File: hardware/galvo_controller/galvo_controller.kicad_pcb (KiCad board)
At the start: 4 copper layers, 70 x 90 mm, 121 parts, among them J1 USB_OTG, J2 Conn_01x03, J3 Conn_01x03, J4 Micro_SD_Card_Det, J5 Red, J6 White, J7 Conn_01x03, J8 Conn_01x03, Q1 MMBT2222, Q2 MMBT2222, U1 SN74LV1T34, U2 ESP-WROOM-32D, U3 CP2104, U4 TPS54295PWP, U5 PCM3060, U6 NCP1117LP, U7 OPA2134, U8 LME49724, U9 LME49724

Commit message: Working on layout
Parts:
- moved JP1 64.2 mm to (163.9, 83.0), turned to 180 degrees
- moved JP2 49.4 mm to (178.0, 105.5), turned to 90 degrees
- moved R9 46.5 mm to (152.2, 117.3), turned to 270 degrees
- moved R15 46.1 mm to (175.4, 111.6), turned to 270 degrees
- moved C4 45.9 mm to (155.7, 112.9), turned to 180 degrees
- moved R18 45.0 mm to (167.0, 111.6), turned to 270 degrees
- moved R5 44.3 mm to (155.1, 85.5), turned to 270 degrees
- moved R14 42.3 mm to (177.2, 111.6), turned to 270 degrees
- moved R17 41.0 mm to (168.8, 111.6), turned to 270 degrees
- moved R7 40.8 mm to (151.3, 85.5), turned to 270 degrees
- moved C26 40.8 mm to (173.0, 111.4), turned to 90 degrees
- moved R13 40.2 mm to (179.0, 111.6), turned to 270 degrees
- moved R8 39.7 mm to (146.4, 117.3), turned to 90 degrees
- moved C2 38.6 mm to (151.5, 112.3)
- moved Q1 38.4 mm to (149.3, 115.3), turned to 90 degrees
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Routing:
- net /SD_DAT1: track 0.00 -> 43.2 mm
- net /SD_CMD: track 0.00 -> 39.2 mm, vias 0 -> 2
- net /SD_DAT0: track 0.00 -> 38.2 mm
- net /VOUTL_N: track 0.00 -> 36.8 mm, vias 0 -> 2
- net /VOUTL_P: track 0.00 -> 35.3 mm
- net /SD_DAT2: track 0.00 -> 32.9 mm, vias 0 -> 2
- net /SD_DAT3: track 0.00 -> 32.3 mm, vias 0 -> 2
- net +3V3: track 3.01 -> 31.3 mm, vias 1 -> 8
- net /SD_CLK: track 0.00 -> 28.0 mm, vias 0 -> 2
- net Net-(JP2-Pad1): track 0.00 -> 17.5 mm, vias 0 -> 2
- net Net-(D2-Pad1): track 0.00 -> 16.7 mm, vias 0 -> 2
- net Net-(D1-Pad1): track 0.00 -> 15.8 mm, vias 0 -> 2
- net /VOUTR_P: track 0.00 -> 14.2 mm
- net /VOUTR_N: track 0.00 -> 14.2 mm
- net /VBUS: track 0.00 -> 12.1 mm, vias 0 -> 2
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
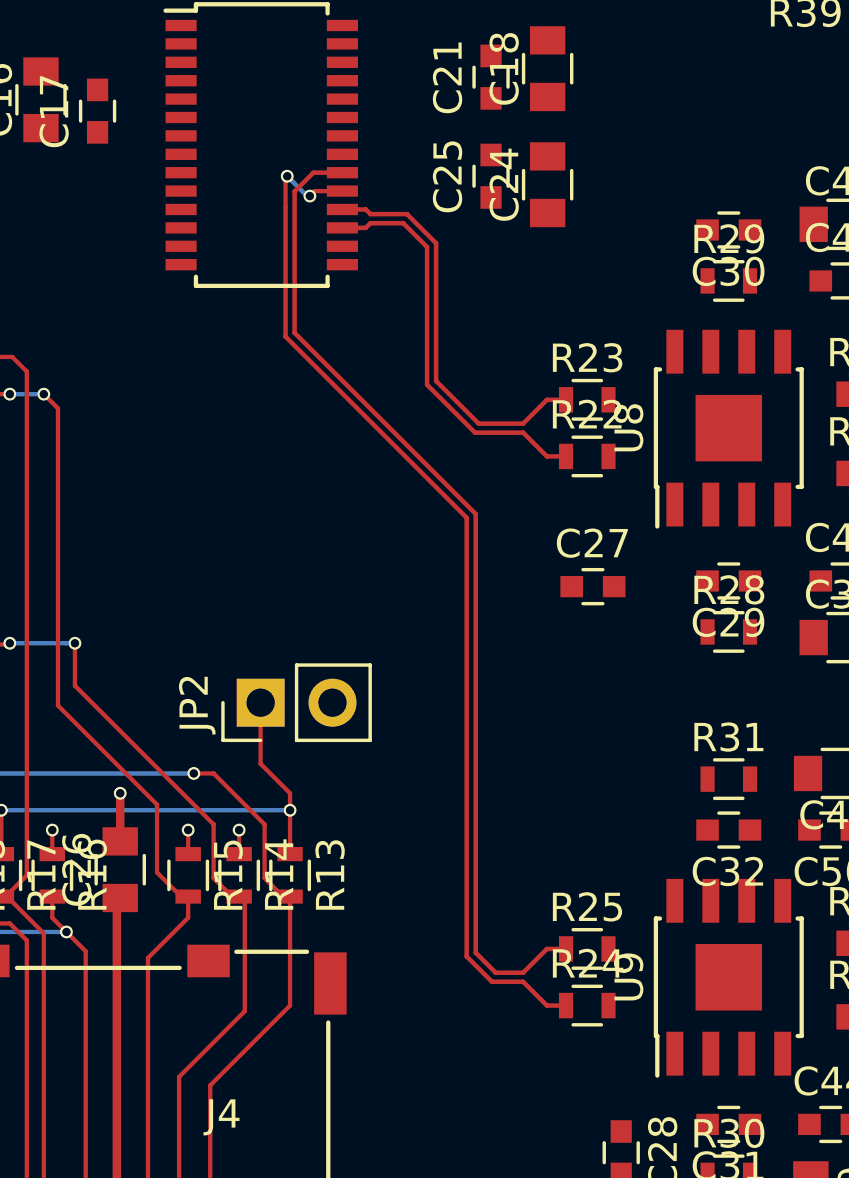
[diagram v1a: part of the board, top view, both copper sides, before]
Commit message: Swapped input L/R channels
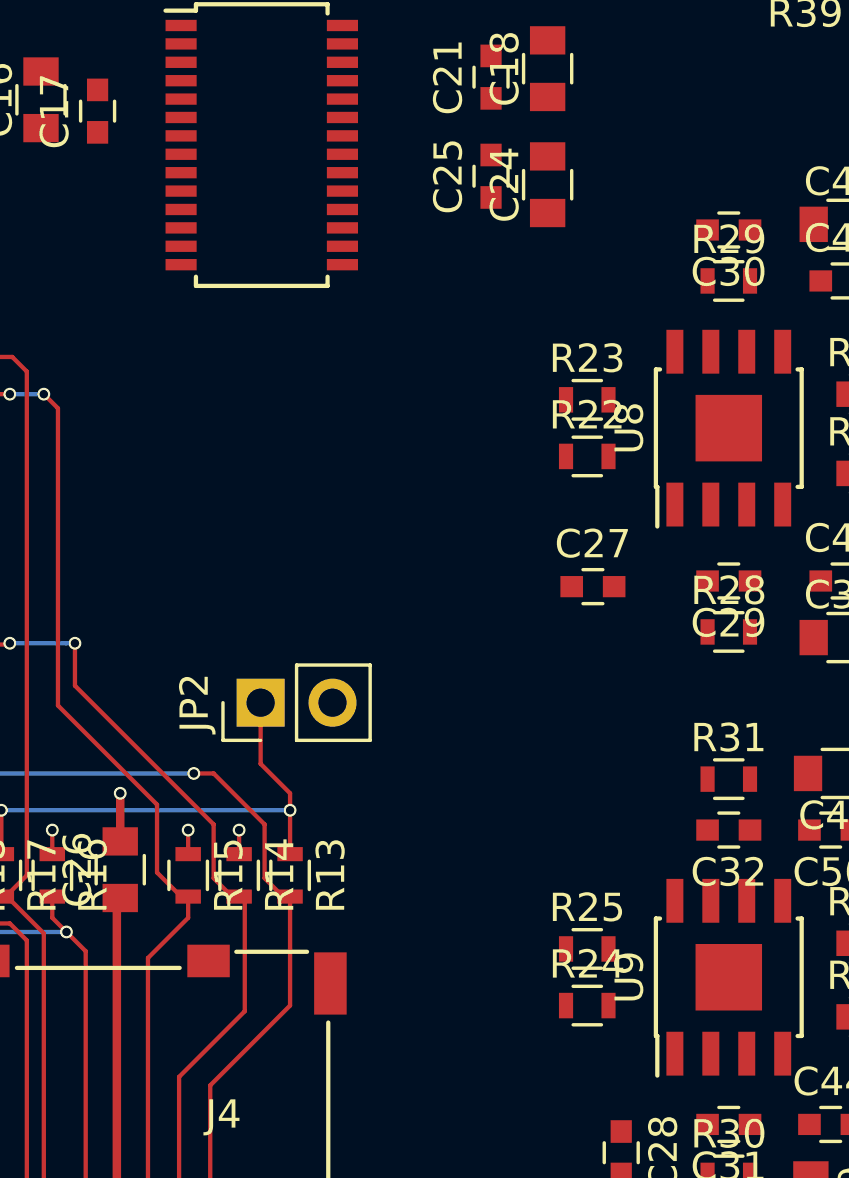
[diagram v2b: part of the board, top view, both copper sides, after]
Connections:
- net Net-(D4-Pad3) renamed /VINR
- net Net-(D5-Pad3) renamed /VINL
- R22 pad 1: /VOUTR_N -> /VOUTL_N
- R23 pad 1: /VOUTR_P -> /VOUTL_P
- R24 pad 1: /VOUTL_N -> /VOUTR_N
- R25 pad 1: /VOUTL_P -> /VOUTR_P
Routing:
- net /VOUTL_N: track 36.8 -> 0.00 mm, vias 2 -> 0
- net /VOUTL_P: track 35.3 -> 0.00 mm
- net /VOUTR_P: track 14.2 -> 0.00 mm
- net /VOUTR_N: track 14.2 -> 0.00 mm

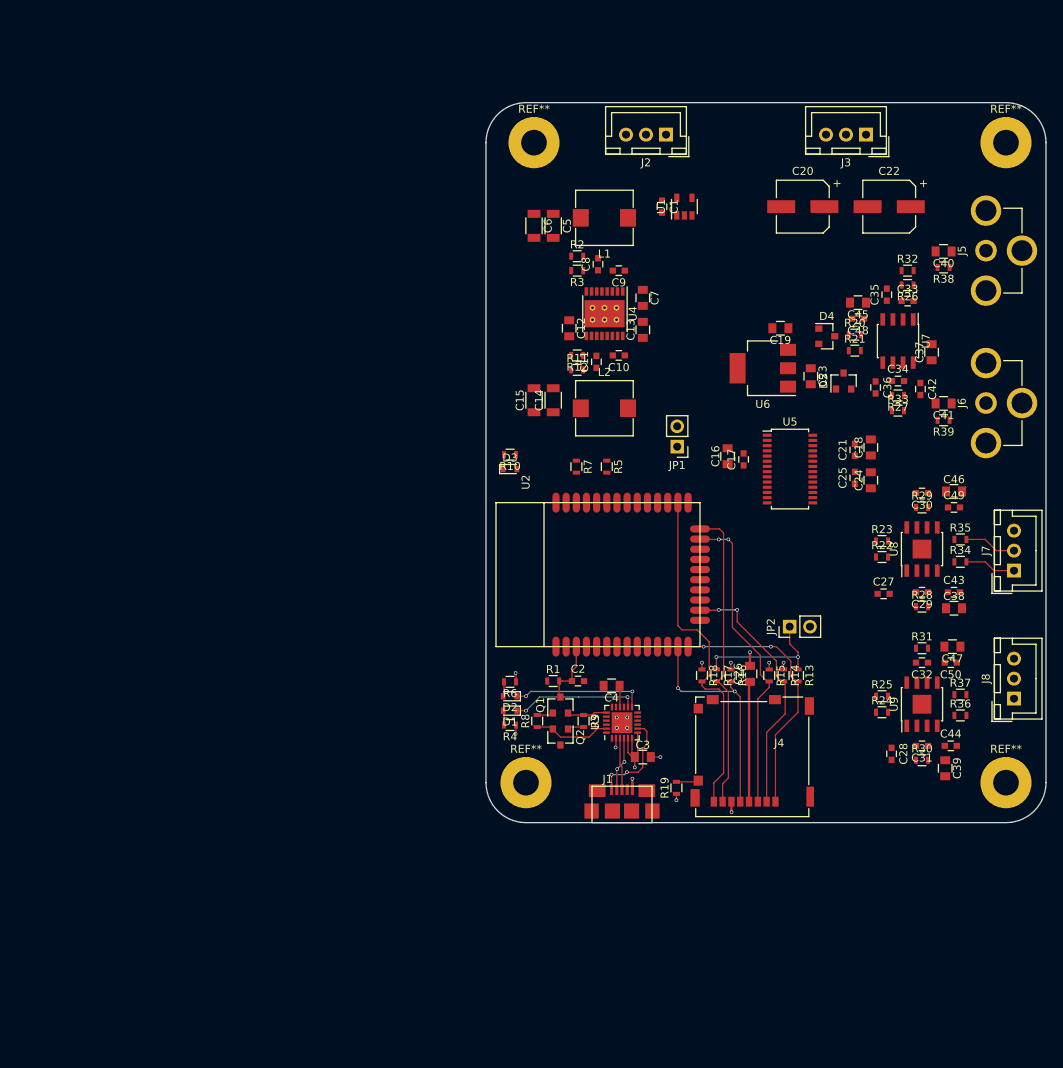
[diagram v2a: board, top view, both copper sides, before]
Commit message: Added OLED and nav switch
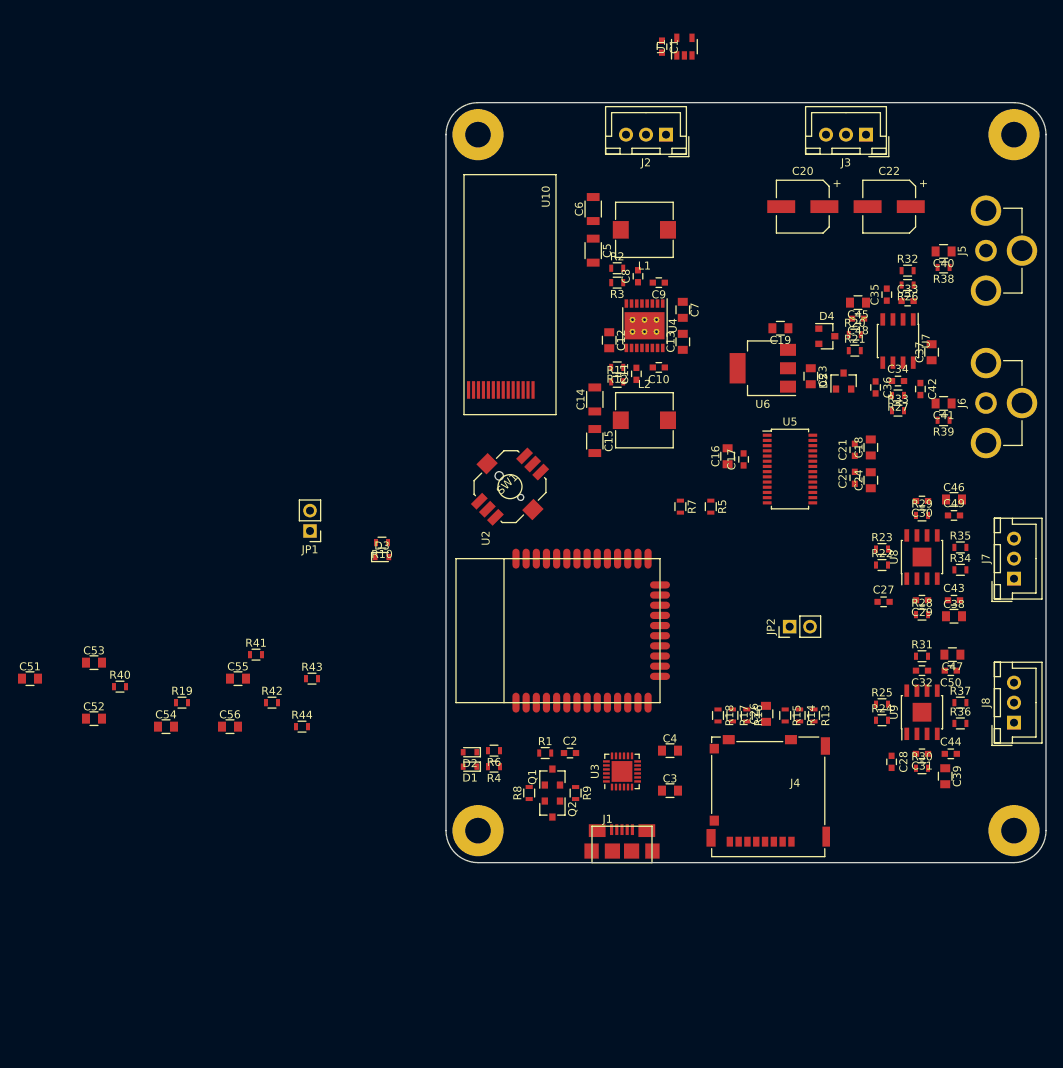
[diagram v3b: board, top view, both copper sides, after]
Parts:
- removed the REF** at (146.0, 45.0)
- removed the REF** at (205.0, 45.0)
- removed the REF** at (205.0, 125.0)
- removed the REF** at (145.0, 125.0)
- added C51: 1u, Capacitors_SMD:C_0805, F.Cu at (83.0, 112.0)
- added C52: 1u, Capacitors_SMD:C_0805, F.Cu at (91.0, 117.0)
- added C53: 10u, Capacitors_SMD:C_0805, F.Cu at (91.0, 110.0)
- added C54: 1u, Capacitors_SMD:C_0805, F.Cu at (100.0, 118.0)
- added C55: 1u, Capacitors_SMD:C_0805, F.Cu at (109.0, 112.0)
- added C56: 10u, Capacitors_SMD:C_0805, F.Cu at (108.0, 118.0)
- added R40: 10k, Resistors_SMD:R_0603, F.Cu at (94.2, 113.0)
- added R41: 10k, Resistors_SMD:R_0603, F.Cu at (111.2, 109.0)
- added R42: 10k, Resistors_SMD:R_0603, F.Cu at (113.2, 115.0)
- added R43: 10k, Resistors_SMD:R_0603, F.Cu at (118.2, 112.0)
- added R44: 10k, Resistors_SMD:R_0603, F.Cu at (117.0, 118.0)
- added REF**: MountingHole_3.2mm_M3_Pad, Mounting_Holes:MountingHole_3.2mm_M3_Pad, F.Cu at (139.0, 131.0)
- added REF**: MountingHole_3.2mm_M3_Pad, Mounting_Holes:MountingHole_3.2mm_M3_Pad, F.Cu at (206.0, 131.0)
- added REF**: MountingHole_3.2mm_M3_Pad, Mounting_Holes:MountingHole_3.2mm_M3_Pad, F.Cu at (206.0, 44.0)
- added REF**: MountingHole_3.2mm_M3_Pad, Mounting_Holes:MountingHole_3.2mm_M3_Pad, F.Cu at (139.0, 44.0)
- added SW1: JS1400BFQ, footprint:JS1400BFQ, F.Cu at (143.0, 88.0)
- added U10: UG-2832HSWEG02, footprint:UG-2832HSWEG02, F.Cu at (143.0, 64.0)
- R19: value 10k -> 390k
- moved R19 62.7 mm to (102.0, 115.0), turned to 0 degrees
- moved JP1 47.1 mm to (118.0, 93.5)
- moved C1 20.0 mm to (162.0, 33.0)
- moved U1 20.0 mm to (164.8, 33.0)
- moved D3 19.4 mm to (127.0, 96.8)
- moved R10 19.4 mm to (127.0, 95.0)
- moved R5 13.9 mm to (168.1, 90.5)
- moved R7 13.9 mm to (164.3, 90.5)
- moved C4 10.9 mm to (163.0, 121.0), turned to 0 degrees
- moved C15 9.15 mm to (153.6, 82.3), turned to 270 degrees
- moved Q2 9.06 mm to (148.3, 128.3)
- moved C2 9.06 mm to (150.5, 121.3)
- moved Q1 9.06 mm to (148.3, 124.3)
- moved R1 9.06 mm to (147.4, 121.3)
- moved R8 9.06 mm to (145.4, 126.3)
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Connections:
- J4 pad 10: /SD_CD -> (no net)
- R19 pad 1: +3V3 -> Net-(R19-Pad1)
- R19 pad 2: /SD_CD -> GNDA
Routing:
- net /SD_DAT1: track 43.2 -> 0.00 mm
- net /SD_CMD: track 39.2 -> 0.00 mm, vias 2 -> 0
- net /SD_DAT0: track 38.2 -> 0.00 mm
- net /SD_DAT2: track 32.9 -> 0.00 mm, vias 2 -> 0
- net /SD_DAT3: track 32.3 -> 0.00 mm, vias 2 -> 0
- net +3V3: track 31.3 -> 0.00 mm, vias 8 -> 0
- net /SD_CLK: track 28.0 -> 0.00 mm, vias 2 -> 0
- net Net-(JP2-Pad1): track 17.5 -> 0.00 mm, vias 2 -> 0
- net Net-(D2-Pad1): track 16.7 -> 0.00 mm, vias 2 -> 0
- net Net-(D1-Pad1): track 15.8 -> 0.00 mm, vias 2 -> 0
- net /VBUS: track 12.1 -> 0.00 mm, vias 2 -> 0
- net /DTR: track 9.63 -> 0.00 mm
- net /RESET: track 8.19 -> 0.00 mm
- net /D_N: track 6.84 -> 0.00 mm, vias 2 -> 0
- net GNDA: track 6.77 -> 0.00 mm, vias 9 -> 0
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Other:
- board size 70 x 90 mm -> 75 x 95 mm

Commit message: Re-annotated schematic
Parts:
- moved C3 18.6 mm to (147.0, 44.0)
- moved U1 18.6 mm to (149.8, 44.0)
- moved SW1 1.00 mm to (143.0, 87.0)
- renumbered C51 to C1, C5 to C10, C2 to C11, C6 to C12, C7 to C13, C8 to C14, C9 to C15, C10 to C16, C11 to C17, C12 to C18, C13 to C19, C52 to C2, C14 to C20, C15 to C21, C16 to C22, C17 to C23, C19 to C24, C20 to C25, C22 to C26, C18 to C27, C21 to C28, C23 to C29, C1 to C3, C24 to C30, C25 to C31, C26 to C32, C27 to C33, C28 to C34, C29 to C35, C30 to C36, C31 to C37, C32 to C38, C33 to C39, C53 to C4, C34 to C40, C35 to C41, C36 to C42, C37 to C43, C38 to C44, C39 to C45, C40 to C46, C41 to C47, C42 to C48, C43 to C49, C54 to C5, C44 to C50, C45 to C51, C46 to C52, C47 to C53, C48 to C54, C49 to C55, C50 to C56, C55 to C6, C56 to C7, C3 to C8, C4 to C9, D3 to D1, D1 to D2, D2 to D3, R10 to R1, R1 to R10, R4 to R11, R6 to R12, R8 to R13, R9 to R14, R5 to R15, R7 to R16, R11 to R17, R12 to R18, R13 to R19, R19 to R2, R14 to R20, R15 to R21, R16 to R22, R17 to R23, R18 to R24, R20 to R25, R21 to R26, R22 to R27, R23 to R28, R24 to R29, R40 to R3, R25 to R30, R26 to R31, R27 to R32, R28 to R33, R29 to R34, R30 to R35, R31 to R36, R32 to R37, R33 to R38, R34 to R39, R41 to R4, R35 to R40, R36 to R41, R37 to R42, R38 to R43, R39 to R44, R42 to R5, R43 to R6, R44 to R7, R2 to R8, R3 to R9, U9 to U10, U10 to U2, U2 to U4, U4 to U5, U5 to U6, U6 to U7, U7 to U8, U8 to U9

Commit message: Working on layout
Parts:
- moved C1 63.7 mm to (137.0, 78.2), turned to 270 degrees
- moved C4 63.3 mm to (148.0, 82.4), turned to 270 degrees
- moved C2 60.8 mm to (140.4, 81.6)
- moved R3 59.6 mm to (148.4, 88.0), turned to 90 degrees
- moved C5 57.3 mm to (137.0, 74.2), turned to 90 degrees
- moved C7 55.2 mm to (150.2, 82.4), turned to 270 degrees
- moved R2 54.9 mm to (145.9, 82.0), turned to 270 degrees
- moved JP1 51.1 mm to (169.0, 97.0), turned to 0 degrees
- moved C6 50.3 mm to (137.0, 70.2), turned to 90 degrees
- moved R5 47.2 mm to (152.0, 88.0), turned to 90 degrees
- moved R7 44.7 mm to (150.2, 88.0), turned to 90 degrees
- moved R4 42.7 mm to (150.2, 91.4), turned to 270 degrees
- moved R6 36.5 mm to (148.4, 91.4), turned to 270 degrees
- moved R1 28.7 mm to (141.0, 120.0)
- moved D1 25.7 mm to (138.0, 120.0)
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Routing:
- net /SD_DAT0: track 0.00 -> 49.2 mm, vias 0 -> 3
- net /GPIO0: track 0.00 -> 47.9 mm, vias 0 -> 2
- net /SD_DAT1: track 0.00 -> 44.8 mm, vias 0 -> 2
- net /SD_DAT2: track 0.00 -> 37.7 mm, vias 0 -> 2
- net /SD_CMD: track 0.00 -> 37.5 mm, vias 0 -> 2
- net /SD_DAT3: track 0.00 -> 32.4 mm, vias 0 -> 2
- net /SD_CLK: track 0.00 -> 32.1 mm, vias 0 -> 2
- net +3V3: track 0.00 -> 30.9 mm, vias 0 -> 5
- net /TXD0: track 0.00 -> 30.5 mm, vias 0 -> 2
- net /RXD0: track 0.00 -> 29.7 mm, vias 0 -> 2
- net /DTR: track 0.00 -> 11.5 mm
- net /VBUS: track 0.00 -> 10.6 mm, vias 0 -> 2
- net Net-(JP2-Pad1): track 0.00 -> 10.3 mm, vias 0 -> 1
- net GNDA: track 0.00 -> 9.23 mm, vias 0 -> 11
- net /RESET: track 0.00 -> 8.95 mm
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
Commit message: Working on layout
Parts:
- moved D1 63.5 mm to (137.0, 56.5), turned to 270 degrees
- moved R1 60.4 mm to (137.0, 59.7), turned to 90 degrees
- moved R16 7.44 mm to (161.6, 87.1)
- moved R15 4.37 mm to (161.6, 90.0), turned to 90 degrees
- moved C22 2.73 mm to (170.6, 86.9), turned to 270 degrees
- moved U5 2.36 mm to (160.7, 65.7)
- moved C13 2.34 mm to (165.4, 63.7)
- moved C14 2.34 mm to (159.8, 59.5)
- moved C15 2.34 mm to (162.4, 60.3)
- moved C19 2.34 mm to (165.4, 67.7)
- moved C21 2.34 mm to (154.4, 80.1)
- moved C10 2.34 mm to (154.2, 56.3)
- moved C17 2.34 mm to (159.6, 71.7)
- moved C18 2.34 mm to (156.2, 67.5)
- moved L2 2.34 mm to (160.6, 77.5)
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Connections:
- J4 pad 11: Net-(J4-Pad11) -> GNDA
- R1 pad 1: (no net) -> /LED
- U1 pad 2: (no net) -> /LASER
- U2 pad 9: (no net) -> /OLED_RST
- U4 pad 10: (no net) -> /LEFT
- U4 pad 11: (no net) -> /LED
- U4 pad 12: (no net) -> /LASER
- U4 pad 27: (no net) -> /I2S_TX
- U4 pad 28: (no net) -> /I2S_MCLK
- U4 pad 29: (no net) -> /I2S_BCLK
- U4 pad 30: (no net) -> /I2S_LRCLK
- U4 pad 31: (no net) -> /I2S_RX
- U4 pad 37: (no net) -> /OLED_RST
- U4 pad 6: (no net) -> /UP
- U4 pad 7: (no net) -> /RIGHT
- U4 pad 8: (no net) -> /SEL
- U4 pad 9: (no net) -> /DOWN
- U6 pad 12: (no net) -> /I2S_TX
- U6 pad 3: (no net) -> /I2S_RX
- U6 pad 4: (no net) -> /I2S_LRCLK
- U6 pad 5: (no net) -> /I2S_BCLK
- U6 pad 6: (no net) -> /I2S_MCLK
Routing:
- net /SCL: track 0.00 -> 60.0 mm, vias 0 -> 2
- net /SDA: track 0.00 -> 58.2 mm, vias 0 -> 2
- net /DOWN: track 0.00 -> 43.1 mm, vias 0 -> 2
- net /LEFT: track 0.00 -> 42.0 mm, vias 0 -> 2
- net /SEL: track 0.00 -> 39.2 mm, vias 0 -> 2
- net /UP: track 0.00 -> 35.5 mm, vias 0 -> 2
- net /RIGHT: track 0.00 -> 34.5 mm, vias 0 -> 2
- net /I2S_RX: track 0.00 -> 33.3 mm
- net /I2S_LRCLK: track 0.00 -> 31.8 mm
- net /I2S_BCLK: track 0.00 -> 30.3 mm
- net /I2S_MCLK: track 0.00 -> 28.8 mm
- net /I2S_TX: track 0.00 -> 22.4 mm
- net /OLED_RST: track 0.00 -> 21.9 mm, vias 0 -> 2
- net +3V3: track 30.9 -> 51.7 mm, vias 5 -> 6
- net GNDA: track 9.23 -> 22.4 mm, vias 11 -> 20
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
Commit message: Working on layout
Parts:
- moved JP1 7.42 mm to (176.0, 99.5)
- moved JP2 5.16 mm to (176.0, 108.5), turned to 180 degrees
- moved R12 2.01 mm to (141.2, 120.0)
- moved D3 2.00 mm to (138.0, 120.0), turned to 0 degrees
- moved R11 1.02 mm to (141.2, 123.0)
- moved D2 1.00 mm to (138.0, 123.0), turned to 0 degrees
- moved C14 0.22 mm to (159.7, 59.7)
- moved C20 0.20 mm to (154.2, 74.9)
- moved C21 0.20 mm to (154.2, 80.1)
- moved C10 0.20 mm to (154.2, 56.5)
- moved C15 0.20 mm to (162.4, 60.5)
- moved R8 0.20 mm to (157.2, 58.7)
- moved R9 0.20 mm to (157.2, 60.5)
- moved C12 0.20 mm to (154.2, 51.3)
- moved L1 0.20 mm to (160.6, 53.9)
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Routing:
- net /LASER: track 0.00 -> 86.0 mm, vias 0 -> 2
- net /LED: track 0.00 -> 68.1 mm, vias 0 -> 2
- net GNDA: track 22.4 -> 56.9 mm, vias 20 -> 49
- net +3V3: track 51.7 -> 81.9 mm, vias 6 -> 16
- net Net-(D2-Pad1): track 0.00 -> 29.1 mm, vias 0 -> 2
- net Net-(D3-Pad1): track 0.00 -> 26.1 mm, vias 0 -> 2
- net +5VD: track 0.00 -> 19.2 mm, vias 0 -> 3
- net VCC: track 0.00 -> 10.5 mm, vias 0 -> 4
- net Net-(C16-Pad2): track 0.00 -> 9.82 mm
- net Net-(C15-Pad2): track 0.00 -> 9.82 mm
- net /GPIO0: track 47.9 -> 55.5 mm
- net Net-(J2-Pad3): track 0.00 -> 7.21 mm
- net Net-(R17-Pad2): track 0.00 -> 4.69 mm
- net Net-(R8-Pad2): track 0.00 -> 4.69 mm
- net /SD_DAT2: track 37.7 -> 34.3 mm
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
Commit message: Working on layout
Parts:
- moved U7 7.55 mm to (176.1, 65.8), turned to 90 degrees
- moved C29 5.96 mm to (175.1, 71.9), turned to 180 degrees
- moved D4 5.70 mm to (181.1, 74.7), turned to 90 degrees
- moved C24 4.61 mm to (181.4, 67.9), turned to 90 degrees
- moved D5 0.51 mm to (185.2, 74.7), turned to 270 degrees
- moved C48 0.45 mm to (193.9, 75.6)
- moved C42 0.40 mm to (189.1, 75.6)
- moved R26 0.30 mm to (186.1, 70.7)
- moved R31 0.20 mm to (192.7, 63.0)
- moved R37 0.20 mm to (192.7, 61.2)
- moved C46 0.10 mm to (197.2, 58.5)
- moved R25 0.10 mm to (186.1, 68.9)
- moved R38 0.10 mm to (191.5, 78.4)
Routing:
- net +5VA: track 0.00 -> 37.9 mm, vias 0 -> 3
- net /VOUTR_N: track 0.00 -> 33.4 mm
- net /VOUTR_P: track 0.00 -> 33.4 mm
- net GNDA: track 56.9 -> 80.1 mm, vias 49 -> 62
- net /VINR: track 0.00 -> 19.6 mm
- net /VOUTL_N: track 0.00 -> 16.1 mm
- net /VOUTL_P: track 0.00 -> 16.1 mm
- net /VINL: track 0.00 -> 16.0 mm
- net VCC: track 10.5 -> 25.3 mm, vias 4 -> 6
- net Net-(C39-Pad2): track 0.00 -> 12.1 mm
- net Net-(C40-Pad2): track 0.00 -> 10.9 mm
- net VEE: track 0.00 -> 10.6 mm, vias 0 -> 1
- net /VCOM: track 0.00 -> 7.28 mm
- net Net-(C39-Pad1): track 0.00 -> 5.98 mm
- net Net-(C40-Pad1): track 0.00 -> 5.95 mm
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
